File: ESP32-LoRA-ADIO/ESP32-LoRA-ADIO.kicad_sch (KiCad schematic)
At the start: 27 parts, among them J1 USB_B_Micro, J2 External Power, J3 AIO/I2C, J4 DIO, J5 RXTX+Power, J6 SMA, Q1 IRLML5203, Q2 2N7002, Q3 2N7002, U1 AP1117-33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

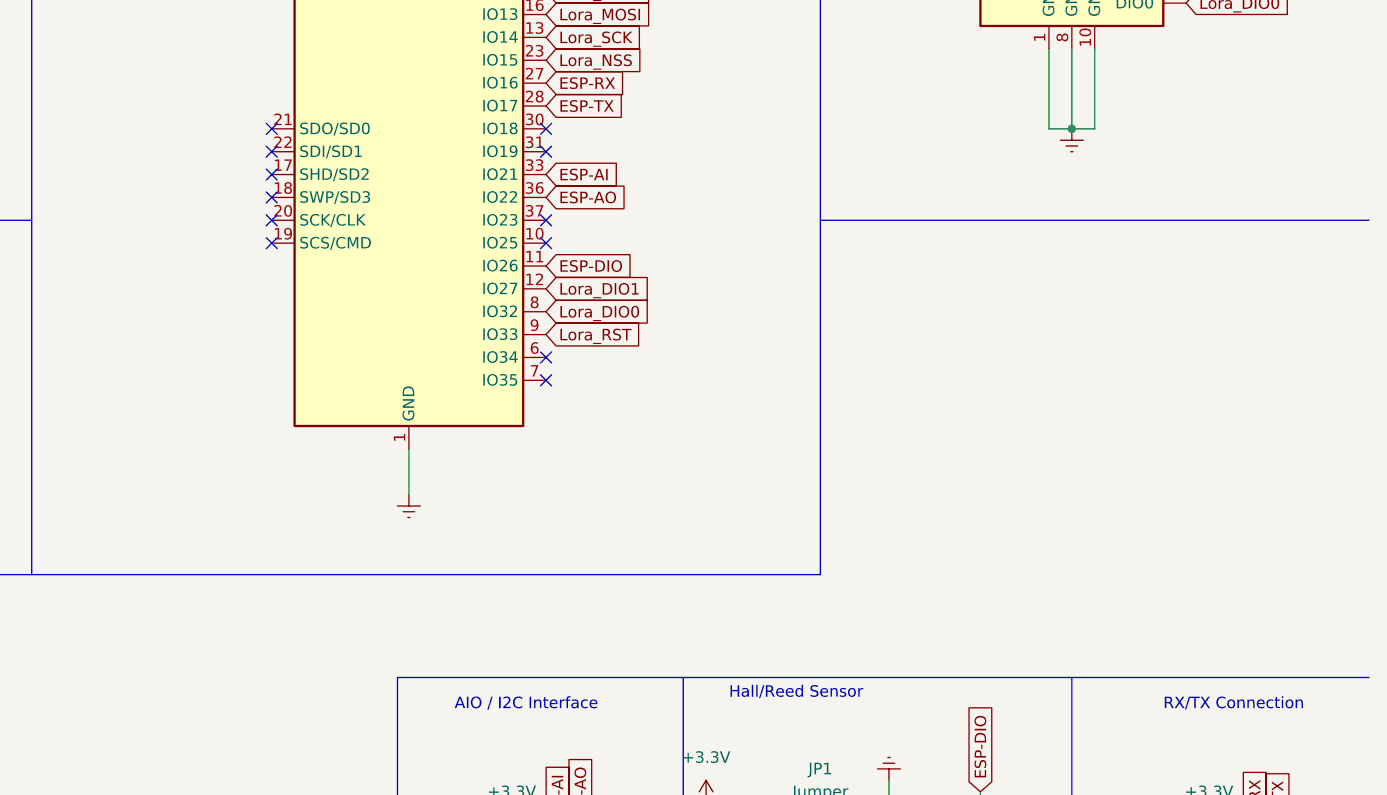
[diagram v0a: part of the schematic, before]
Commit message: Add JTAG debug interface to schematics
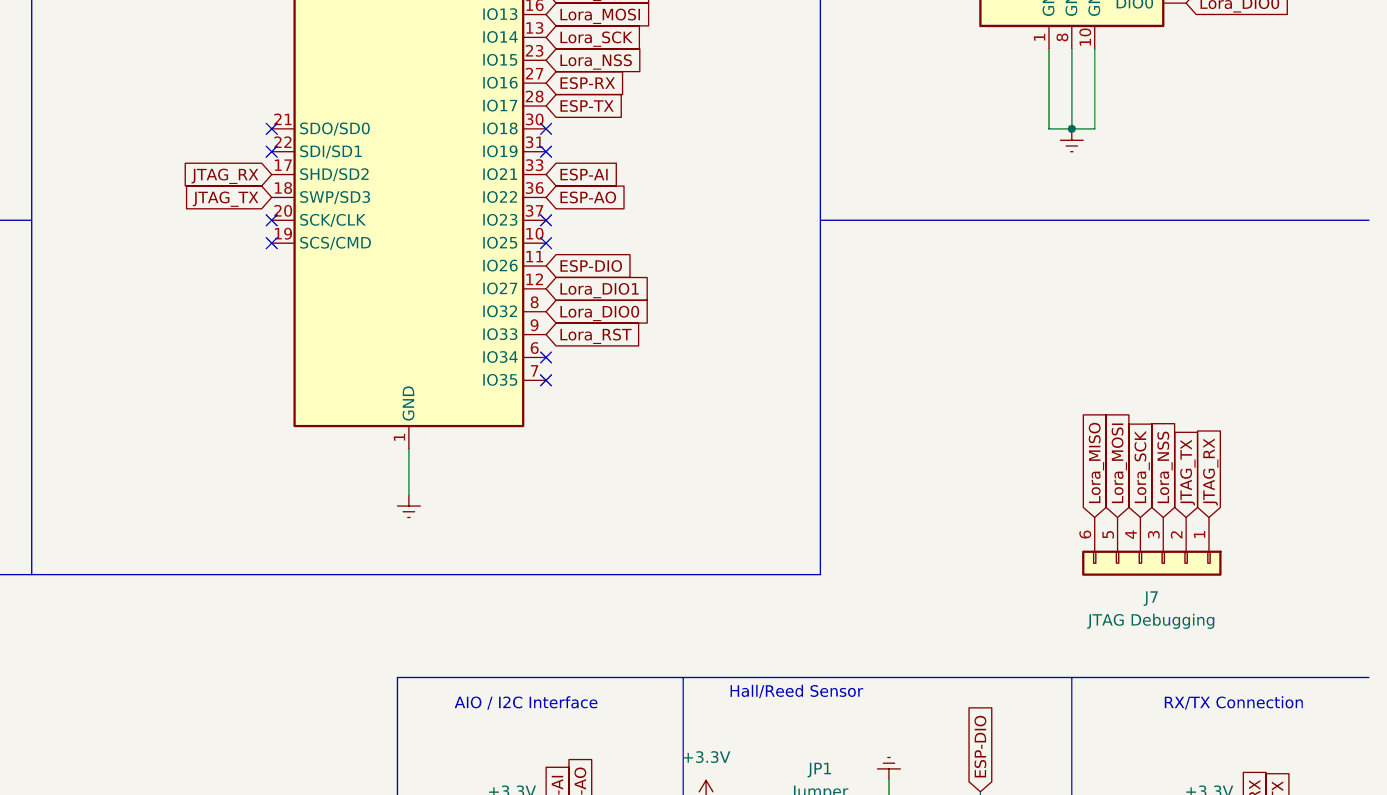
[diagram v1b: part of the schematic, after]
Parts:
- added J7: JTAG Debugging, Connector_JST:JST_XH_B6B-XH-A_1x06_P2.50mm_Vertical, symbol Connector_Generic:Conn_01x06
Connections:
- net Lora_MISO: now also J7.6 (Pin_6)
- net Lora_MOSI: now also J7.5 (Pin_5)
- net Lora_NSS: now also J7.3 (Pin_3)
- net Lora_SCK: now also J7.4 (Pin_4)
- net JTAG_RX: now reaches U3.17 (SHD/SD2)
- net JTAG_RX: now also J7.1 (Pin_1)
- net JTAG_TX: now reaches U3.18 (SWP/SD3)
- net JTAG_TX: now also J7.2 (Pin_2)
- no-connect marks 25 -> 23
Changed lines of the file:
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@@
   (no_connect (at 162.56 76.2))
   (no_connect (at 162.56 66.04))
-  (no_connect (at 162.56 68.58))
-  (no_connect (at 162.56 71.12))
   (no_connect (at 264.16 36.83))
   (no_connect (at 264.16 39.37))
@@
     )
   )
+  (global_label "Lora_MISO" (shape input) (at 254 106.68 90) (fields_autoplaced)
+    (effects (font (size 1.27 1.27)) (justify left))
+    (property "Intersheet References" "${INTERSHEET_REFS}" (id 0) (at 199.39 281.94 0)
+      (effects (font (size 1.27 1.27)) hide)
+    )
+  )
   (global_label "USB-D-" (shape input) (at 97.79 45.72 180) (fields_autoplaced)
     (effects (font (size 1.27 1.27)) (justify right))
@@
     )
   )
+  (global_label "Lora_MOSI" (shape input) (at 256.54 106.68 90) (fields_autoplaced)
+    (effects (font (size 1.27 1.27)) (justify left))
+    (property "Intersheet References" "${INTERSHEET_REFS}" (id 0) (at 199.39 281.94 0)
+      (effects (font (size 1.27 1.27)) hide)
+    )
+  )
   (global_label "ESP-TX" (shape input) (at 274.32 143.51 90) (fields_autoplaced)
     (effects (font (size 1.27 1.27)) (justify left))
@@
     )
   )
+  (global_label "Lora_NSS" (shape input) (at 261.62 106.68 90) (fields_autoplaced)
+    (effects (font (size 1.27 1.27)) (justify left))
+    (property "Intersheet References" "${INTERSHEET_REFS}" (id 0) (at 199.39 281.94 0)
+      (effects (font (size 1.27 1.27)) hide)
+    )
+  )
   (global_label "ESP-AI" (shape input) (at 193.04 68.58 0) (fields_autoplaced)
     (effects (font (size 1.27 1.27)) (justify left))
@@
     )
   )
+  (global_label "JTAG_TX" (shape input) (at 162.56 71.12 180) (fields_autoplaced)
+    (effects (font (size 1.27 1.27)) (justify right))
+    (property "Intersheet References" "${INTERSHEET_REFS}" (id 0) (at 152.7972 71.1994 0)
+      (effects (font (size 1.27 1.27)) (justify right) hide)
+    )
+  )
+  (global_label "JTAG_TX" (shape input) (at 264.16 106.68 90) (fields_autoplaced)
+    (effects (font (size 1.27 1.27)) (justify left))
+    (property "Intersheet References" "${INTERSHEET_REFS}" (id 0) (at 264.0806 96.9172 90)
+      (effects (font (size 1.27 1.27)) (justify left) hide)
+    )
+  )
   (global_label "DTR" (shape input) (at 95.25 95.25 180) (fields_autoplaced)
     (effects (font (size 1.27 1.27)) (justify right))
@@
     )
   )
+  (global_label "JTAG_RX" (shape input) (at 266.7 106.68 90) (fields_autoplaced)
+    (effects (font (size 1.27 1.27)) (justify left))
+    (property "Intersheet References" "${INTERSHEET_REFS}" (id 0) (at 266.6206 96.6148 90)
+      (effects (font (size 1.27 1.27)) (justify left) hide)
+    )
+  )
   (global_label "ESP-RX" (shape input) (at 271.78 143.51 90) (fields_autoplaced)
     (effects (font (size 1.27 1.27)) (justify left))
@@
     )
   )
+  (global_label "JTAG_RX" (shape input) (at 162.56 68.58 180) (fields_autoplaced)
+    (effects (font (size 1.27 1.27)) (justify right))
+    (property "Intersheet References" "${INTERSHEET_REFS}" (id 0) (at 152.4948 68.6594 0)
+      (effects (font (size 1.27 1.27)) (justify right) hide)
+    )
+  )
   (global_label "ESP-TX" (shape input) (at 193.04 60.96 0) (fields_autoplaced)
     (effects (font (size 1.27 1.27)) (justify left))
@@
     )
   )
+  (global_label "Lora_SCK" (shape input) (at 259.08 106.68 90) (fields_autoplaced)
+    (effects (font (size 1.27 1.27)) (justify left))
+    (property "Intersheet References" "${INTERSHEET_REFS}" (id 0) (at 199.39 281.94 0)
+      (effects (font (size 1.27 1.27)) hide)
+    )
+  )
   (global_label "ESP-AI" (shape input) (at 194.31 142.24 90) (fields_autoplaced)
     (effects (font (size 1.27 1.27)) (justify left))
@@
     (pin "2")
   )
+  (symbol (lib_id "Connector_Generic:Conn_01x06") (at 261.62 111.76 270) (unit 1)
+    (in_bom yes) (on_board yes)
+    (property "Reference" "J7" (id 0) (at 260.35 115.57 90))
+    (property "Value" "JTAG Debugging" (id 1) (at 260.35 118.11 90))
+    (property "Footprint" "Connector_JST:JST_XH_B6B-XH-A_1x06_P2.50mm_Vertical" (id 2) (at 261.62 111.76 0)
+      (effects (font (size 1.27 1.27)) hide)
+    )
+    (property "Datasheet" "~" (id 3) (at 261.62 111.76 0)
+      (effects (font (size 1.27 1.27)) hide)
+    )
+    (pin "1")
+    (pin "2")
+    (pin "3")
+    (pin "4")
+    (pin "5")
+    (pin "6")
+  )
   (symbol (lib_id "Connector_Generic:Conn_01x04") (at 194.31 153.67 270) (unit 1)
     (in_bom yes) (on_board yes) (fields_autoplaced)
@@
       (reference "J6") (unit 1) (value "SMA") (footprint "Connector_Coaxial:SMA_Amphenol_901-144_Vertical")
     )
+    (path "/7e1180a9-9908-4f35-acb9-3bb1fe31a0e9"
+      (reference "J7") (unit 1) (value "JTAG Debugging") (footprint "Connector_JST:JST_XH_B6B-XH-A_1x06_P2.50mm_Vertical")
+    )
     (path "/24977d6b-17e2-4e15-941b-3effcd13bf2d"

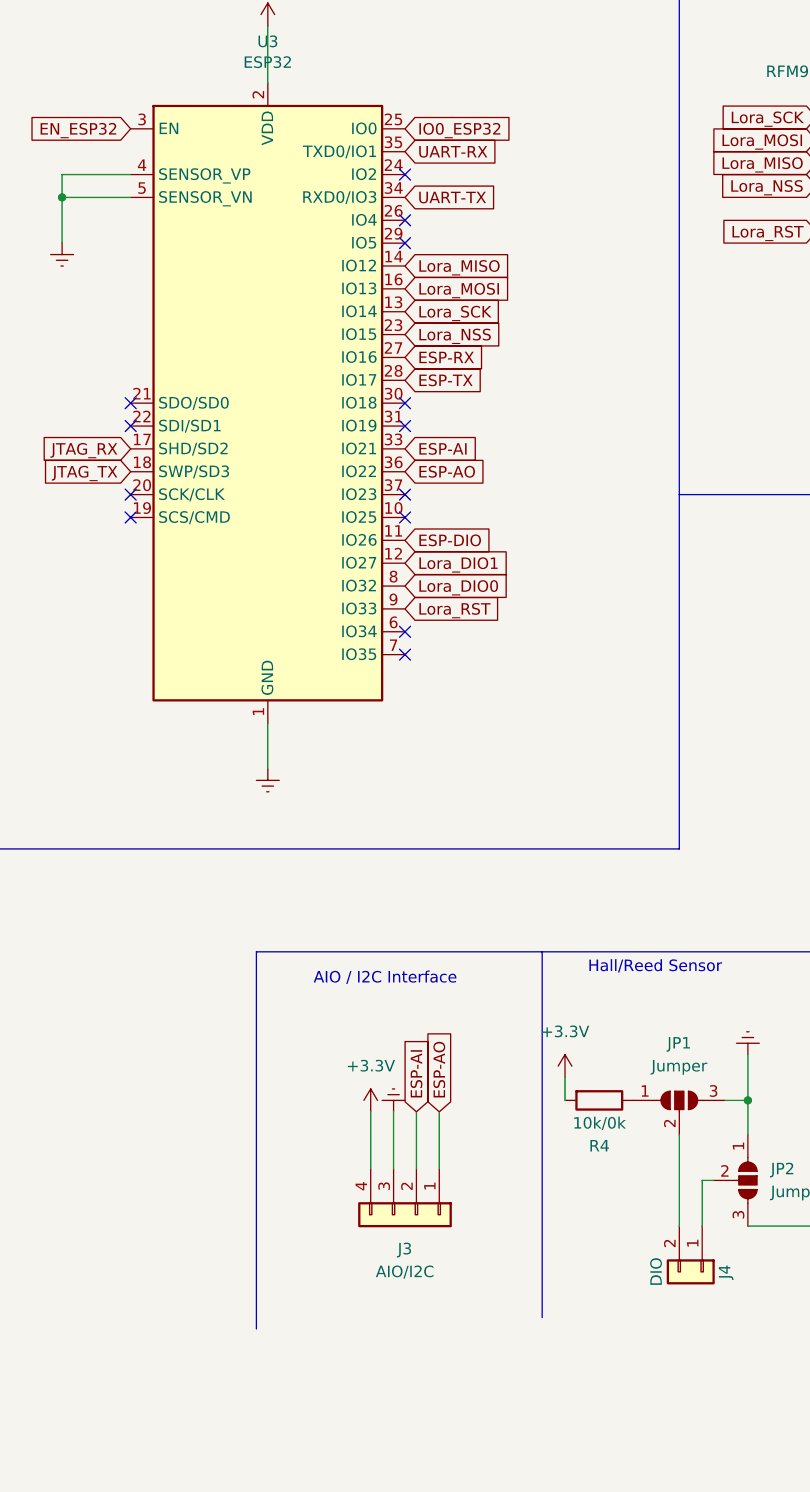
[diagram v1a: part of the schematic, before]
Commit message: Add a AI and add jumpers to the AI/I2C slot
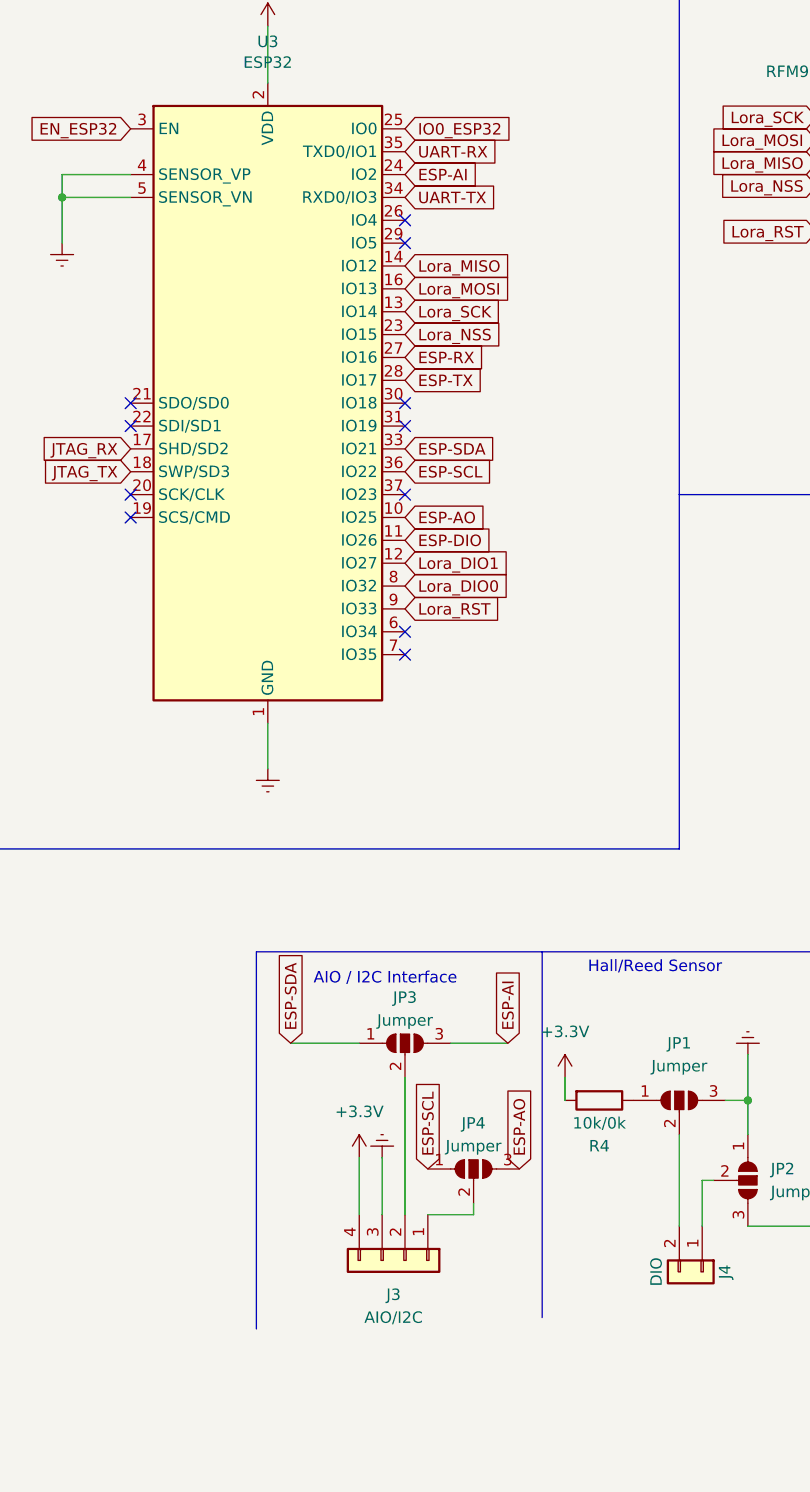
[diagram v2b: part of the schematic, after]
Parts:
- added JP3, JP4: Jumper, Jumper:SolderJumper-3_P1.3mm_Open_Pad1.0x1.5mm, symbol Jumper:SolderJumper_3_Open
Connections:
- net ESP-AI: now also U3.24 (IO2), JP3.3 (B); no longer J3.2 (Pin_2), U3.33 (IO21)
- net ESP-AO: now also U3.10 (IO25), JP4.3 (B); no longer J3.1 (Pin_1), U3.36 (IO22)
- new net: J3.1 (Pin_1), JP4.2 (C)
- new net: J3.2 (Pin_2), JP3.2 (C)
- new net ESP-SCL: JP4.1 (A), U3.36 (IO22)
- new net ESP-SDA: JP3.1 (A), U3.33 (IO21)
- no-connect marks 23 -> 21
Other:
- moved on the sheet: J3
